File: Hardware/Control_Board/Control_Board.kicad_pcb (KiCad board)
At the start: 0 parts

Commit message: took measurements, need to make contact switch for silicon footprint
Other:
- board outline added: 56.4 x 140 mm
- copper layers 0 -> 2
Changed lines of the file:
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@@
 (kicad_pcb
-  (version 20260206)
-  (generator "pcbnew")
-  (generator_version "10.0"))
+	(version 20260206)
+	(generator "pcbnew")
+	(generator_version "10.0")
+	(general
+		(thickness 1.6)
+		(legacy_teardrops no)
+	)
+	(paper "A4")
+	(layers
+		(0 "F.Cu" signal)
+		(2 "B.Cu" signal)
+		(9 "F.Adhes" user "F.Adhesive")
+		(11 "B.Adhes" user "B.Adhesive")
+		(13 "F.Paste" user)
+		(15 "B.Paste" user)
+		(5 "F.SilkS" user "F.Silkscreen")
+		(7 "B.SilkS" user "B.Silkscreen")
+		(1 "F.Mask" user)
+		(3 "B.Mask" user)
+		(17 "Dwgs.User" user "User.Drawings")
+		(19 "Cmts.User" user "User.Comments")
+		(21 "Eco1.User" user "User.Eco1")
+		(23 "Eco2.User" user "User.Eco2")
+		(25 "Edge.Cuts" user)
+		(27 "Margin" user)
+		(31 "F.CrtYd" user "F.Courtyard")
+		(29 "B.CrtYd" user "B.Courtyard")
+		(35 "F.Fab" user)
+		(33 "B.Fab" user)
+		(39 "User.1" user)
+		(41 "User.2" user)
+		(43 "User.3" user)
+		(45 "User.4" user)
+	)
+	(setup
+		(pad_to_mask_clearance 0)
+		(allow_soldermask_bridges_in_footprints no)
+		(tenting
+			(front yes)
+			(back yes)
+		)
+		(covering
+			(front no)
+			(back no)
+		)
+		(plugging
+			(front no)
+			(back no)
+		)
+		(capping no)
+		(filling no)
+		(pcbplotparams
+			(layerselection 0x00000000_00000000_55555555_5755f5ff)
+			(plot_on_all_layers_selection 0x00000000_00000000_00000000_00000000)
+			(disableapertmacros no)
+			(usegerberextensions no)
+			(usegerberattributes yes)
+			(usegerberadvancedattributes yes)
+			(creategerberjobfile yes)
+			(dashed_line_dash_ratio 12)
+			(dashed_line_gap_ratio 3)
+			(svgprecision 4)
+			(plotframeref no)
+			(mode 1)
+			(useauxorigin no)
+			(pdf_front_fp_property_popups yes)
+			(pdf_back_fp_property_popups yes)
+			(pdf_metadata yes)
+			(pdf_single_document no)
+			(dxfpolygonmode yes)
+			(dxfimperialunits yes)
+			(dxfusepcbnewfont yes)
+			(psnegative no)
+			(psa4output no)
+			(plot_black_and_white yes)
+			(sketchpadsonfab no)
+			(plotpadnumbers no)
+			(hidednponfab no)
+			(sketchdnponfab yes)
+			(crossoutdnponfab yes)
+			(subtractmaskfromsilk no)
+			(outputformat 1)
+			(mirror no)
+			(drillshape 1)
+			(scaleselection 1)
+			(outputdirectory "")
+		)
+	)
+	(gr_line
+		(start 99.7 36.9)
+		(end 99.7 162.9)
+		(stroke
+			(width 0.05)
+			(type default)
+		)
+		(layer "Edge.Cuts")
+	)
+	(gr_line
+		(start 99.7 36.9)
+		(end 119.7 36.9)
+		(stroke
+			(width 0.05)
+			(type default)
+		)
+		(layer "Edge.Cuts")
+	)
+	(gr_line
+		(start 119.7 36.9)
+		(end 156.1 176.9)
+		(stroke
+			(width 0.05)
+			(type default)
+		)
+		(layer "Edge.Cuts")
+	)
+	(gr_line
+		(start 125.1 176.9)
+		(end 99.7 162.9)
+		(stroke
+			(width 0.05)
+			(type default)
+		)
+		(layer "Edge.Cuts")
+	)
+	(gr_line
+		(start 125.1 176.9)
+		(end 156.1 176.9)
+		(stroke
+			(width 0.05)
+			(type default)
+		)
+		(layer "Edge.Cuts")
+	)
+	(embedded_fonts no)
+)

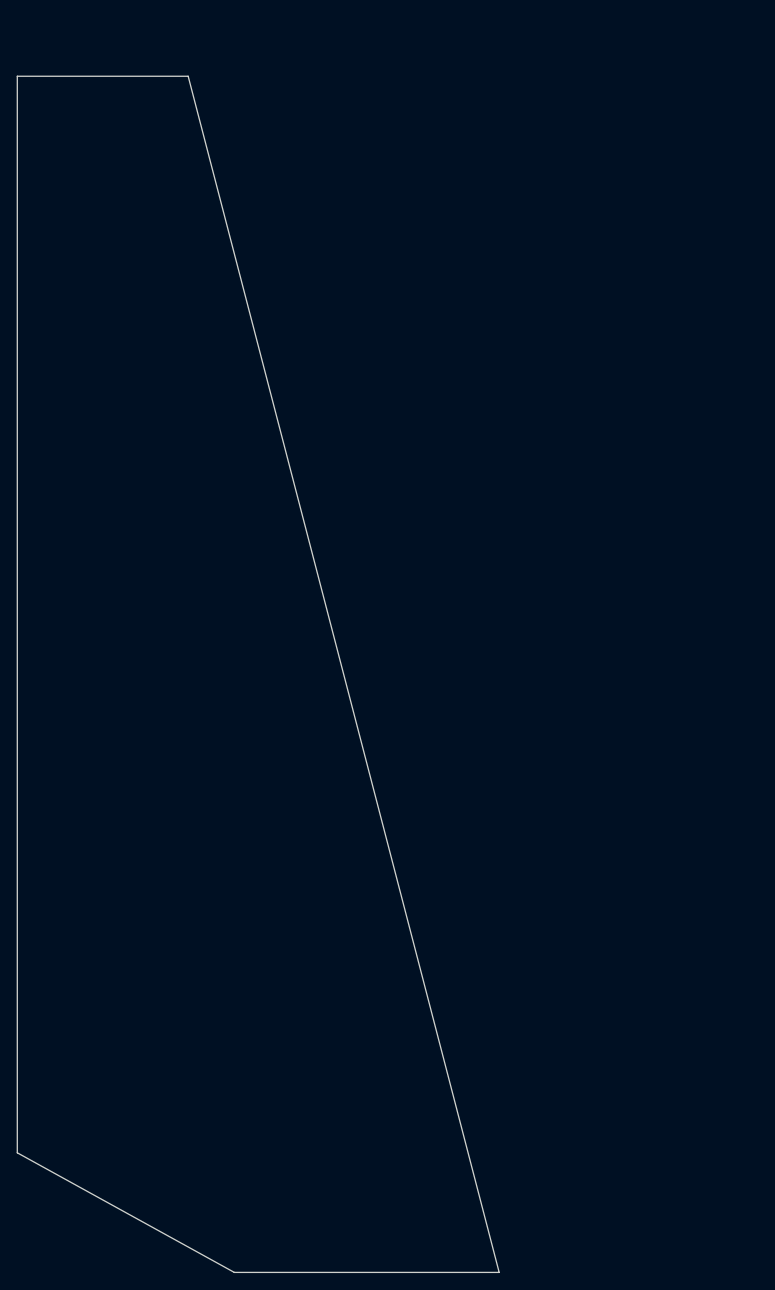
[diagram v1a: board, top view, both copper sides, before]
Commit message: made contact switch footprints + LED through hole footprints
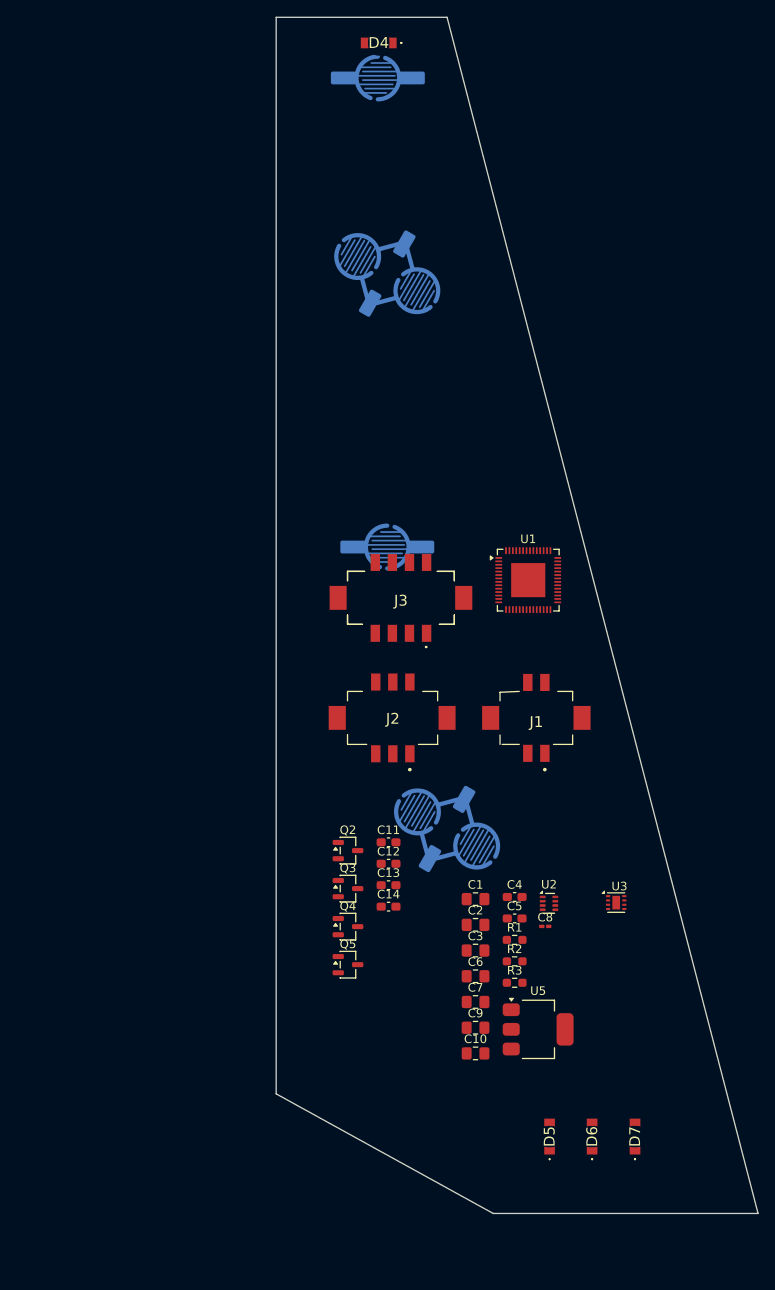
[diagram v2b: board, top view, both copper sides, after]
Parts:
- added C1: 10uF, Capacitor_SMD:C_0805_2012Metric_Pad1.18x1.45mm_HandSolder, F.Cu at (153.3, 133.2)
- added C10: 2.2uF, Capacitor_SMD:C_0805_2012Metric_Pad1.18x1.45mm_HandSolder, F.Cu at (153.3, 151.3)
- added C11: 100nF, Capacitor_SMD:C_0603_1608Metric_Pad1.08x0.95mm_HandSolder, F.Cu at (143.2, 126.6)
- added C12: 100nF, Capacitor_SMD:C_0603_1608Metric_Pad1.08x0.95mm_HandSolder, F.Cu at (143.2, 129.1)
- added C13: 100nF, Capacitor_SMD:C_0603_1608Metric_Pad1.08x0.95mm_HandSolder, F.Cu at (143.2, 131.6)
- added C14: 100nF, Capacitor_SMD:C_0603_1608Metric_Pad1.08x0.95mm_HandSolder, F.Cu at (143.2, 134.1)
- added C2: 10uF, Capacitor_SMD:C_0805_2012Metric_Pad1.18x1.45mm_HandSolder, F.Cu at (153.3, 136.2)
- added C3: 10uF, Capacitor_SMD:C_0805_2012Metric_Pad1.18x1.45mm_HandSolder, F.Cu at (153.3, 139.2)
- added C4: 33nF, Capacitor_SMD:C_0603_1608Metric_Pad1.08x0.95mm_HandSolder, F.Cu at (157.9, 133.0)
- added C5: 100nF, Capacitor_SMD:C_0603_1608Metric_Pad1.08x0.95mm_HandSolder, F.Cu at (157.9, 135.5)
- added C6: 22uF, Capacitor_SMD:C_0805_2012Metric_Pad1.18x1.45mm_HandSolder, F.Cu at (153.3, 142.2)
- added C7: 22uF, Capacitor_SMD:C_0805_2012Metric_Pad1.18x1.45mm_HandSolder, F.Cu at (153.3, 145.2)
- added C8: 100nF, Capacitor_SMD:C_0201_0603Metric_Pad0.64x0.40mm_HandSolder, F.Cu at (161.5, 136.4)
- added C9: 1uF, Capacitor_SMD:C_0805_2012Metric_Pad1.18x1.45mm_HandSolder, F.Cu at (153.3, 148.3)
- added D4: LED, Meow:LED_1204_Hole, F.Cu at (142.0, 33.0)
- added D5: LED, Meow:LED_1204_Hole, F.Cu at (162.0, 161.0)
- added D6: LED, Meow:LED_1204_Hole, F.Cu at (167.0, 161.0)
- added D7: LED, Meow:LED_1204_Hole, F.Cu at (172.0, 161.0)
- added J1: DF11CZ-4DP-2V_27_, Meow:DF11CZ4DP2V27, F.Cu at (160.4, 112.0)
- added J2: DF11CZ-4DP-2V_27_, Meow:DF11CZ6DP2V27, F.Cu at (143.7, 112.0)
- added J3: DF11CZ-8DP-2V_27_, Meow:DF11CZ8DP2V27, F.Cu at (144.6, 98.0)
- added Q2: 2N7002, Package_TO_SOT_SMD:SOT-23-3, F.Cu at (138.4, 127.5)
- added Q3: 2N7002, Package_TO_SOT_SMD:SOT-23-3, F.Cu at (138.4, 132.0)
- added Q4: 2N7002, Package_TO_SOT_SMD:SOT-23-3, F.Cu at (138.4, 136.4)
- added Q5: 2N7002, Package_TO_SOT_SMD:SOT-23-3, F.Cu at (138.4, 140.9)
- added R1: 10k, Resistor_SMD:R_0603_1608Metric_Pad0.98x0.95mm_HandSolder, F.Cu at (157.9, 138.0)
- added R2: 52.3k, Resistor_SMD:R_0603_1608Metric_Pad0.98x0.95mm_HandSolder, F.Cu at (157.9, 140.5)
- added R3: 51.1k, Resistor_SMD:R_0603_1608Metric_Pad0.98x0.95mm_HandSolder, F.Cu at (157.9, 143.0)
- added SW1: Power, Meow:Contact_Switch_5mm, B.Cu at (141.9, 37.1)
- added SW2: Cycle, Meow:Contact_Switch_5mm_Double, B.Cu at (143.0, 60.0)
- added SW3: Empty, Meow:Contact_Switch_5mm, B.Cu at (143.0, 92.0)
- added SW4: Reset, Meow:Contact_Switch_5mm_Double, B.Cu at (150.0, 125.0)
- added U1: ESP32-S2, Package_DFN_QFN:QFN-56-1EP_7x7mm_P0.4mm_EP4x4mm, F.Cu at (159.5, 95.9)
- added U2: TPS62933, Package_TO_SOT_SMD:SOT-583-8, F.Cu at (161.9, 133.7)
- added U3: DRV8231ADSG, Package_SON:WSON-8-1EP_2x2mm_P0.5mm_EP0.9x1.6mm, F.Cu at (169.8, 133.6)
- added U5: TLV76133DCY, Package_TO_SOT_SMD:SOT-223-3_TabPin2, F.Cu at (160.7, 148.5)
